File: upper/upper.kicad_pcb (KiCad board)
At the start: 2 copper layers, 1 part, among them U1 RaspberryPi_Pico_W

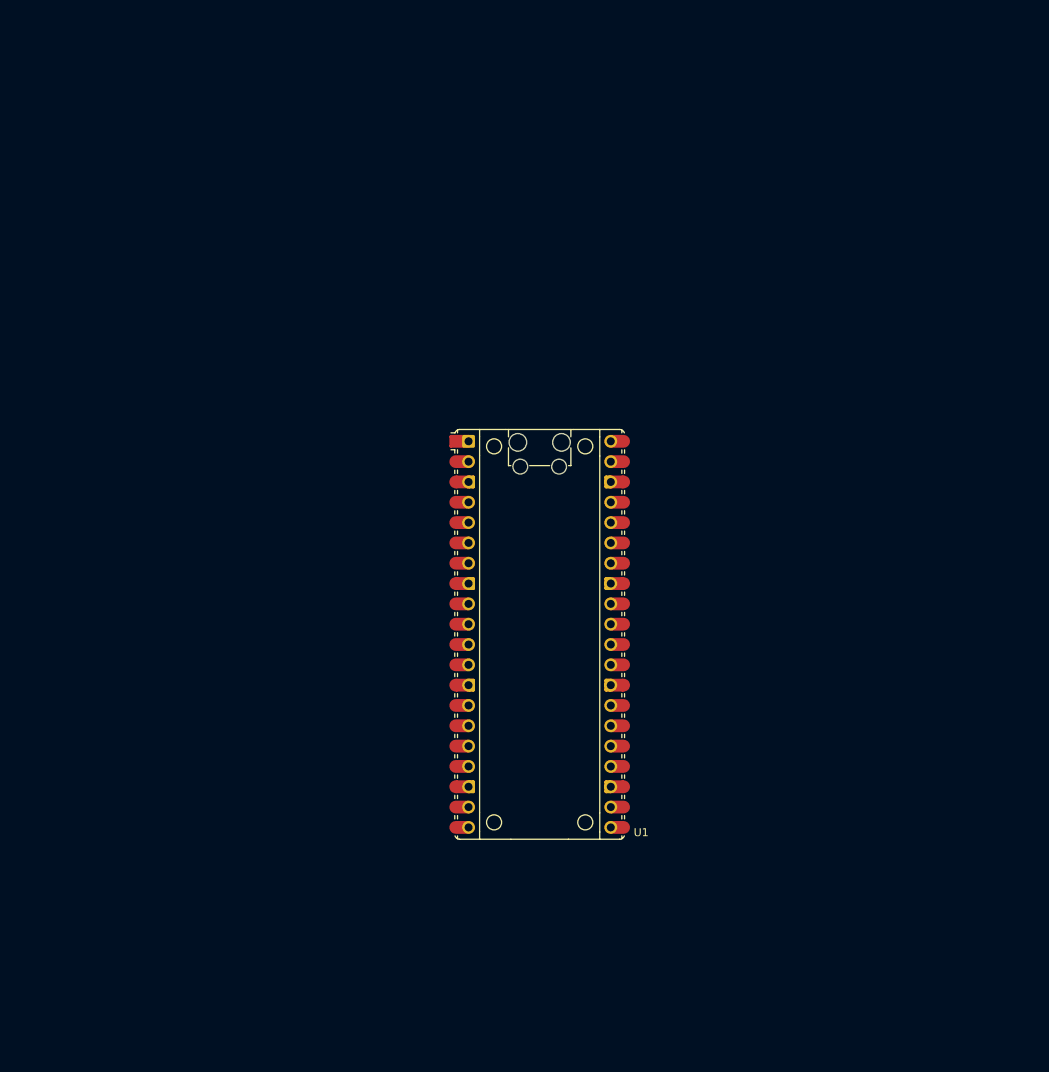
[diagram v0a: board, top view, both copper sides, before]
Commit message: Quick lower PCB for cost estimation
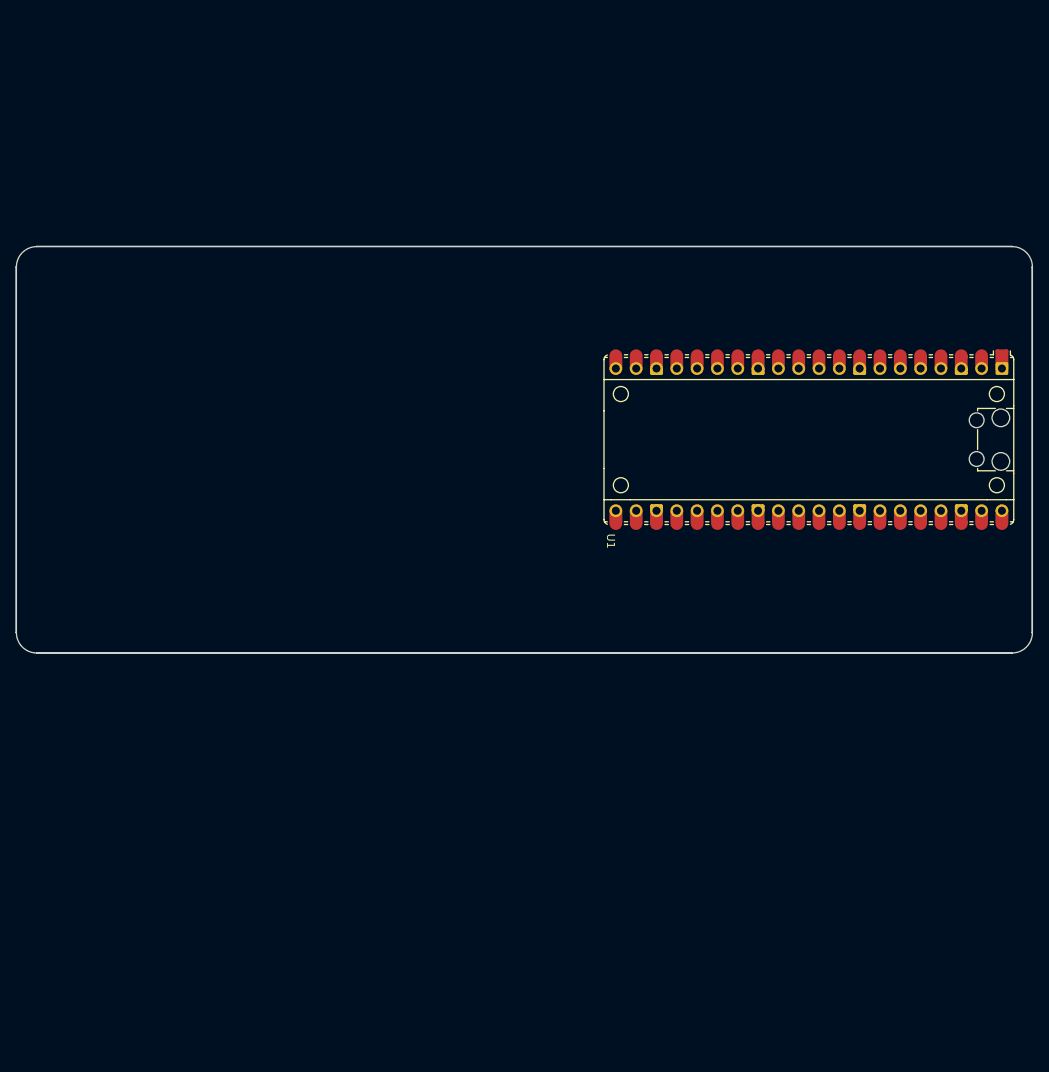
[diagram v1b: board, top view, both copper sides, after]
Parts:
- moved U1 41.5 mm to (175.3, 74.9), turned to -90 degrees
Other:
- board outline added: 127 x 50.8 mm

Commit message: Upper v0.0.1. Pre-routed
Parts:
- added H1: MountingHole, MountingHole:MountingHole_3.2mm_M3_ISO14580, F.Cu at (164.2, 27.0)
- added H2: MountingHole, MountingHole:MountingHole_3.2mm_M3_ISO14580, F.Cu at (164.2, 148.0)
- added H3: MountingHole, MountingHole:MountingHole_3.2mm_M3_ISO14580, F.Cu at (130.2, 148.0)
- added H4: MountingHole, MountingHole:MountingHole_3.2mm_M3_ISO14580, F.Cu at (130.2, 27.0)
- moved U1 38.9 mm to (147.2, 48.0), turned to 0 degrees
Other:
- board size 127 x 50.8 mm -> 50 x 130 mm

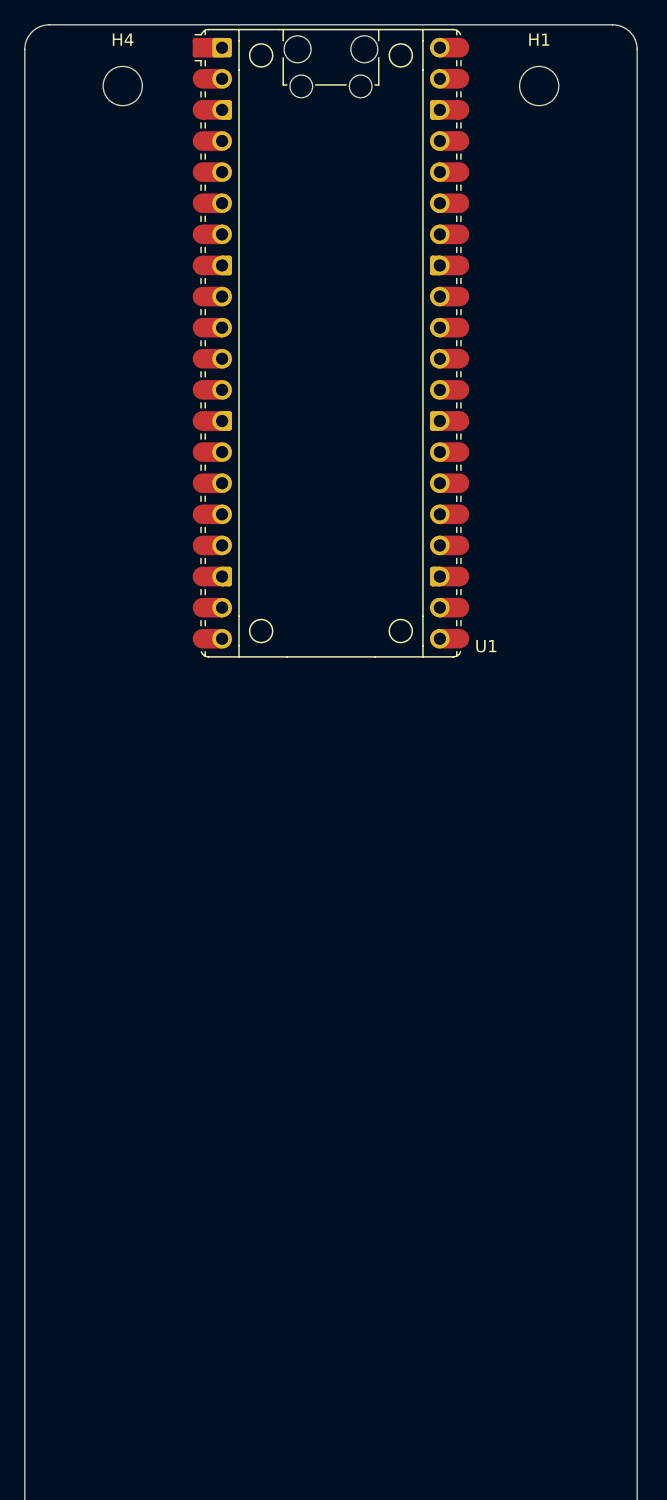
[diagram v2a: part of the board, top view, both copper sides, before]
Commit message: Upper v0.1.0. Pre-routed
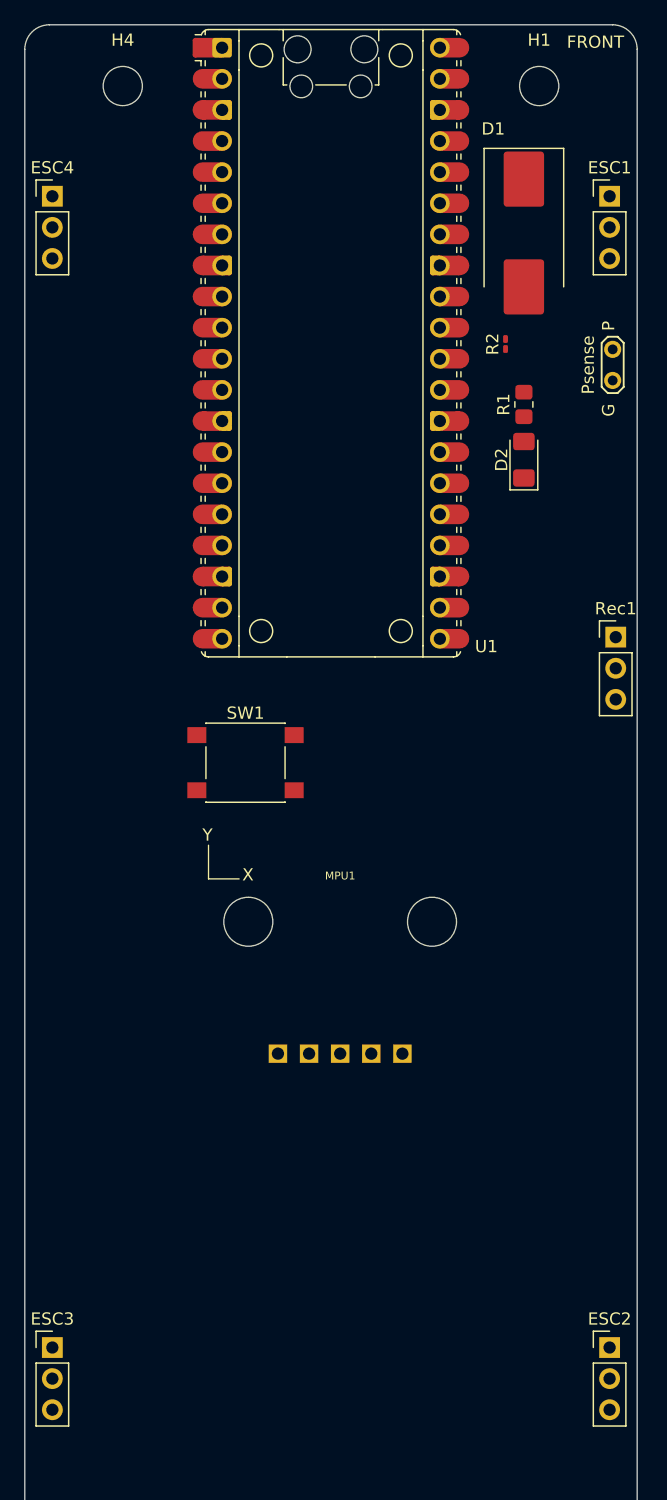
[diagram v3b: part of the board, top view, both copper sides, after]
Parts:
- added D1: 1N5822, Diode_SMD:D_SMC_Handsoldering, F.Cu at (163.0, 39.0)
- added D2: LED, LED_SMD:LED_1206_3216Metric_Pad1.42x1.75mm_HandSolder, F.Cu at (163.0, 57.5)
- added ESC1: ~, Connector_PinHeader_2.54mm:PinHeader_1x03_P2.54mm_Vertical, F.Cu at (170.0, 36.0)
- added ESC2: ~, Connector_PinHeader_2.54mm:PinHeader_1x03_P2.54mm_Vertical, F.Cu at (170.0, 130.0)
- added ESC3: ~, Connector_PinHeader_2.54mm:PinHeader_1x03_P2.54mm_Vertical, F.Cu at (124.5, 130.0)
- added ESC4: ~, Connector_PinHeader_2.54mm:PinHeader_1x03_P2.54mm_Vertical, F.Cu at (124.5, 36.0)
- added MPU1: MPU-6050, SEN0142:SEN0142, F.Cu at (148.0, 104.7)
- added R1: 330, Resistor_SMD:R_0805_2012Metric_Pad1.20x1.40mm_HandSolder, F.Cu at (163.0, 53.0)
- added R2: 510, Resistor_SMD:R_0201_0603Metric_Pad0.64x0.40mm_HandSolder, F.Cu at (161.5, 48.1)
- added Rec1: ~, Connector_PinHeader_2.54mm:PinHeader_1x03_P2.54mm_Vertical, F.Cu at (170.5, 72.0)
- added SW1: SW_Push, Button_Switch_SMD:SW_Push_1P1T_NO_6x6mm_H9.5mm, F.Cu at (140.3, 82.2)
- added TP1: Psense, TestPoint:TestPoint_2Pads_Pitch2.54mm_Drill0.8mm, F.Cu at (170.2, 48.5)
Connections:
- net Net-(U1-GND-Pad13) renamed GND
- U1 pad 1: unconnected-(U1-GPIO0-Pad1) -> /M1
- U1 pad 11: unconnected-(U1-GPIO8-Pad11) -> /SDA
- U1 pad 12: unconnected-(U1-GPIO9-Pad12) -> /SCL
- U1 pad 21: unconnected-(U1-GPIO16-Pad21) -> /PPM
- U1 pad 29: unconnected-(U1-GPIO22-Pad29) -> Net-(U1-GPIO22)
- U1 pad 30: unconnected-(U1-RUN-Pad30) -> Net-(U1-RUN)
- U1 pad 31: unconnected-(U1-GPIO26_ADC0-Pad31) -> /Psense
- U1 pad 32: unconnected-(U1-GPIO27_ADC1-Pad32) -> /Res?
- U1 pad 36: unconnected-(U1-3V3-Pad36) -> +3.3V
- U1 pad 39: unconnected-(U1-VSYS-Pad39) -> Net-(D1-K)
- U1 pad 4: unconnected-(U1-GPIO2-Pad4) -> /M2
- U1 pad 6: unconnected-(U1-GPIO4-Pad6) -> /M3
- U1 pad 9: unconnected-(U1-GPIO6-Pad9) -> /M4
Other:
- board text added: "FRONT"
- board text added: "G"
- board text added: "P"

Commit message: Upper/Lower: v0.2.0. Pre-routed
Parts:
- removed R2: 510, Resistor_SMD:R_0201_0603Metric_Pad0.64x0.40mm_HandSolder
- added BMP1: Adafruit-BMP280, upper-all:adafruit-bmp280, F.Cu at (148.2, 119.8)
- added JP1: Jumper_2_Open, Jumper:SolderJumper-2_P1.3mm_Open_RoundedPad1.0x1.5mm, F.Cu at (170.0, 44.5)
- added JP2: Jumper_2_Bridged, Jumper:SolderJumper-2_P1.3mm_Bridged_RoundedPad1.0x1.5mm, F.Cu at (169.8, 138.5)
- added JP3: Jumper_2_Open, Jumper:SolderJumper-2_P1.3mm_Open_RoundedPad1.0x1.5mm, F.Cu at (124.7, 138.5)
- added JP4: Jumper_2_Open, Jumper:SolderJumper-2_P1.3mm_Open_RoundedPad1.0x1.5mm, F.Cu at (124.5, 44.5)
- added TP2: Vsense, TestPoint:TestPoint_2Pads_Pitch2.54mm_Drill0.8mm, F.Cu at (170.2, 56.5)
- TP1: value Psense -> Isense
- moved TP1 1.75 mm to (170.2, 50.2)
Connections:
- net /Psense renamed /Isense
- ESC1 pad 2: +5V -> Net-(ESC1-Pin_2)
- ESC2 pad 2: +5V -> Net-(ESC2-Pin_2)
- ESC3 pad 2: +5V -> Net-(ESC3-Pin_2)
- ESC4 pad 2: +5V -> Net-(ESC4-Pin_2)
- U1 pad 32: /Res? -> /Vsense
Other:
- board text added: "NC"
- board text added: "S"
- board text removed: "P"

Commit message: Upper/Lower: v0.2.0. Routed
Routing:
- net GND: track 0.00 -> 276.7 mm
- net +5V: track 0.00 -> 212.1 mm
- net /M2: track 0.00 -> 118.3 mm
- net +3.3V: track 0.00 -> 105.2 mm, vias 0 -> 1
- net /M3: track 0.00 -> 99.6 mm
- net /SCL: track 0.00 -> 97.3 mm
- net /SDA: track 0.00 -> 84.0 mm, vias 0 -> 1
- net Net-(U1-RUN): track 0.00 -> 48.1 mm, vias 0 -> 1
- net /M1: track 0.00 -> 37.3 mm
- net /M4: track 0.00 -> 20.8 mm
- net /Vsense: track 0.00 -> 19.2 mm
- net /Isense: track 0.00 -> 15.6 mm
- net /PPM: track 0.00 -> 14.4 mm
- net Net-(D1-K): track 0.00 -> 11.4 mm
- net Net-(U1-GPIO22): track 0.00 -> 6.94 mm
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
